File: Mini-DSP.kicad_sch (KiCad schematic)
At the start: 74 parts, among them J1 9V, J2 Barrel_Jack_MountingPin, J3 MOBO_Con, SW1 USB_BOOT, SW2 USB_BOOT, U1 CS4270, U2 AMS1117-3.3, U3 W25Q128JVS, U4 AMS1117-5.0, U5 APS1604M-3SQRx-SN, U6 RP2350A-QFN60, Y1 ABM8-272-T3

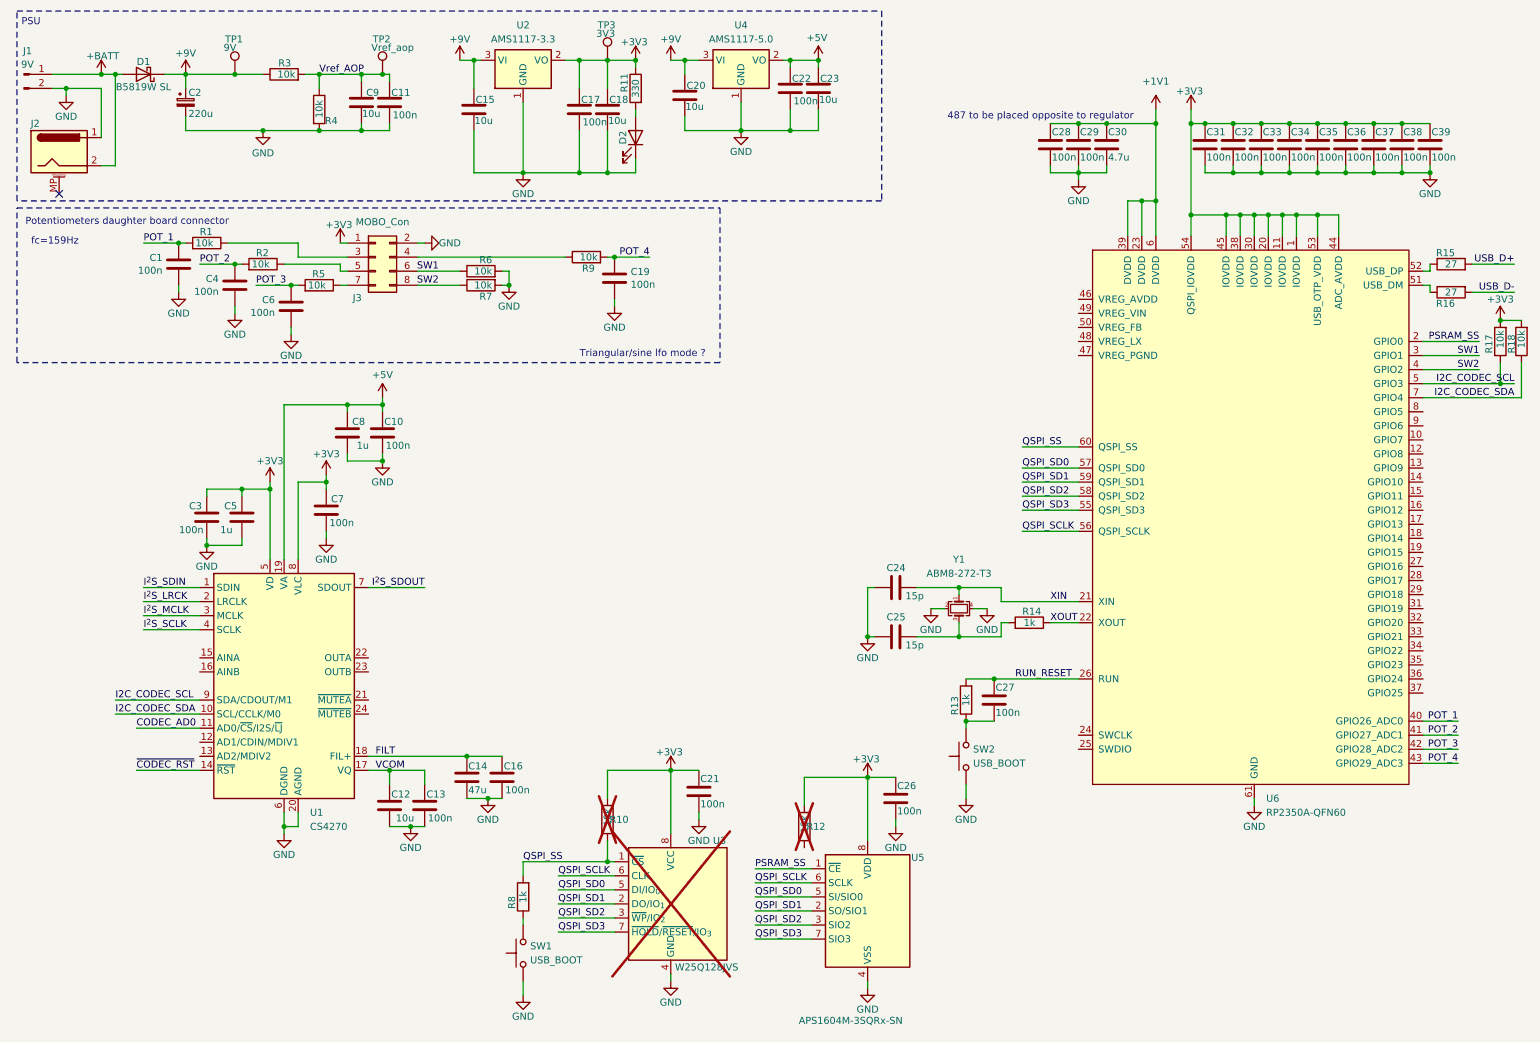
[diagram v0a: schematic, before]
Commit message: update schematic and placement
- missing 3PDT part
- need to change CS4270 (EoL)
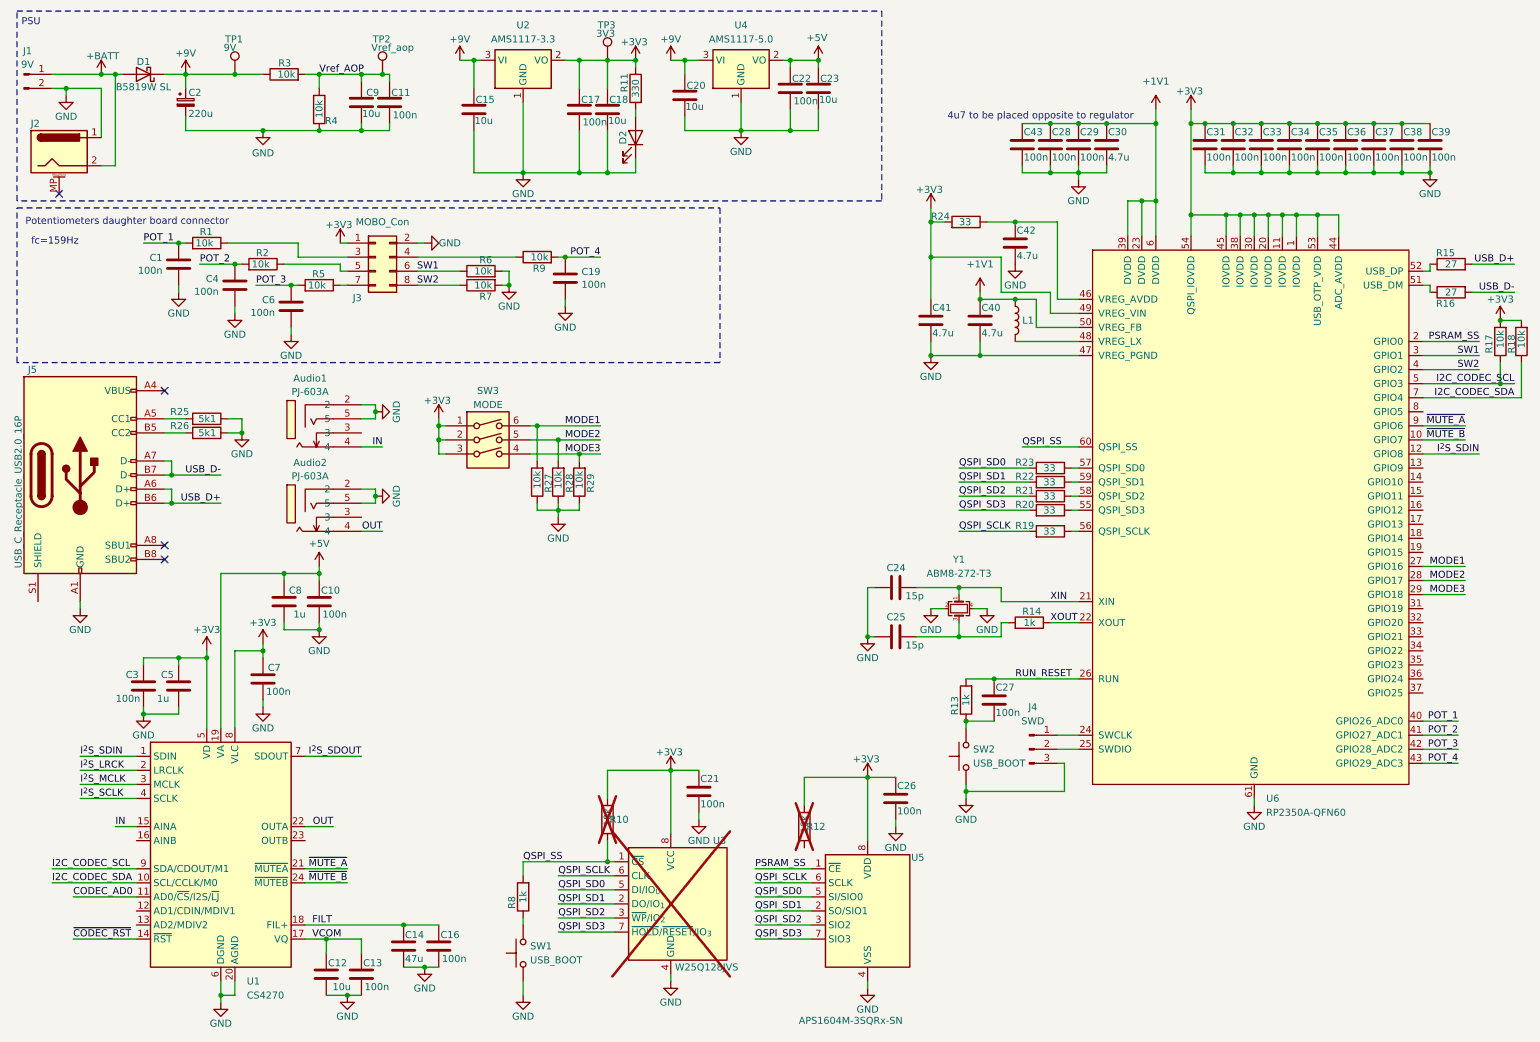
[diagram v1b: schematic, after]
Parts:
- added Audio1, Audio2: PJ-603A, easyeda2kicad:AUDIO-TH_PJ-603A, symbol easyeda2kicad:PJ-603A
- added C40, C41, C42: 4.7u, Capacitor_SMD:C_0402_1005Metric, symbol Device:C
- added C43: 100n, Capacitor_SMD:C_0402_1005Metric, symbol Device:C
- added J4: SWD, Connector_PinHeader_1.27mm:PinHeader_1x03_P1.27mm_Vertical, symbol Connector:Conn_01x03_Pin
- added J5: USB_C_Receptacle_USB2.0_16P, Connector_USB:USB_C_Receptacle_HCTL_HC-TYPE-C-16P-01A, symbol Connector:USB_C_Receptacle_USB2.0_16P
- added L1: AOTA-B201610S3R3-101-T, Inductor_SMD:L_Murata_DFE201610P, symbol Device:L
- added R19, R20, R21, R22, R23, R24: 33, Resistor_SMD:R_0402_1005Metric, symbol Device:R
- added R25, R26: 5k1, Resistor_SMD:R_0402_1005Metric, symbol Device:R
- added R27, R28, R29: 10k, Resistor_SMD:R_0402_1005Metric, symbol Device:R
- added SW3: MODE, Button_Switch_SMD:SW_DIP_SPSTx03_Slide_KingTek_DSHP03TS_W7.62mm_P1.27mm, symbol Switch:SW_DIP_x03
- C1, C11, C17, C19, C22, C4, C6: footprint Capacitor_SMD:C_0603_1608Metric -> Capacitor_SMD:C_0402_1005Metric
- C10, C13, C16, C3, C7: footprint Capacitor_SMD:C_0805_2012Metric -> Capacitor_SMD:C_0402_1005Metric
- R1, R10, R11, R12, R13, R14, R15, R16, R17, R18, R2, R3, R4, R5, R6, R7, R8, R9: footprint Resistor_SMD:R_0603_1608Metric -> Resistor_SMD:R_0402_1005Metric
- U6: footprint (none) -> Package_DFN_QFN:QFN-60-1EP_7x7mm_P0.4mm_EP3.4x3.4mm_ThermalVias
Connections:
- net +1V1: now also U6.50 (VREG_FB), C40.1, C43.1, L1.1
- net +3V3: now also U6.49 (VREG_VIN), C41.1, R24.2, SW3.1, SW3.2, SW3.3
- net GND: now also U6.47 (VREG_PGND), Audio1.2, Audio1.5, Audio2.2, Audio2.5, C40.2, C41.2, C42.2, C43.2, J4.3 (Pin_3), J5.A1 (GND), J5.A12 (GND), J5.B1 (GND), J5.B12 (GND), R25.1, R26.1, R27.1, R28.1, R29.1
- net I^{2}S_SDIN: now also U6.12 (GPIO8)
- net QSPI_SCLK: now also R19.2; no longer U6.56 (QSPI_SCLK)
- net QSPI_SD0: now also R23.2; no longer U6.57 (QSPI_SD0)
- net QSPI_SD1: now also R22.2; no longer U6.59 (QSPI_SD1)
- net QSPI_SD2: now also R21.2; no longer U6.58 (QSPI_SD2)
- net QSPI_SD3: now also R20.2; no longer U6.55 (QSPI_SD3)
- net USB_D+: now also J5.A6 (D+), J5.B6 (D+)
- net USB_D-: now also J5.A7 (D-), J5.B7 (D-)
- net ~{MUTE_B}: now reaches U6.10 (GPIO7)
- net ~{MUTE_B}: now also U1.24 (~{MUTEB})
- net at U6.24 (SWCLK): now also J4.1 (Pin_1)
- net at U6.25 (SWDIO): now also J4.2 (Pin_2)
- net MODE1: now reaches U6.27 (GPIO16)
- net MODE1: now also R27.2, SW3.6
- net MODE2: now reaches U6.28 (GPIO17)
- net MODE2: now also R28.2, SW3.5
- net MODE3: now reaches U6.29 (GPIO18)
- net MODE3: now also R29.2, SW3.4
- net at U6.46 (VREG_AVDD): now also C42.1, R24.1
- net at U6.48 (VREG_LX): now also L1.2
- net ~{MUTE_A}: now reaches U6.9 (GPIO6)
- net ~{MUTE_A}: now also U1.21 (~{MUTEA})
- net IN: now reaches U1.15 (AINA)
- net IN: now also Audio1.4
- net OUT: now reaches U1.22 (OUTA)
- net OUT: now also Audio2.4
- new net: R19.1, U6.56 (QSPI_SCLK)
- new net: R20.1, U6.55 (QSPI_SD3)
- new net: R23.1, U6.57 (QSPI_SD0)
- new net: R21.1, U6.58 (QSPI_SD2)
- new net: R22.1, U6.59 (QSPI_SD1)
- new net: J5.B5 (CC2), R26.2
- new net: J5.A4 (VBUS), J5.A9 (VBUS), J5.B4 (VBUS), J5.B9 (VBUS)
- new net: J5.A5 (CC1), R25.2
- no-connect marks 1 -> 4
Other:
- note added: "4u7 to be placed opposite to regulator"
- note removed: "487 to be placed opposite to regulator"
- note removed: "Triangular/sine lfo mode ?"
- moved on the sheet: C10, C12, C13, C14, C16, C19, C3, C5, C7, C8, R9, U1

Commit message: WIP
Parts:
- removed C22: 100n, Capacitor_SMD:C_0402_1005Metric, symbol Device:C
- removed C23: 10u, Capacitor_SMD:C_0805_2012Metric, symbol Device:C
- removed U1: CS4270, Package_SO:TSSOP-24_4.4x7.8mm_P0.65mm, symbol Audio:CS4270
- removed U4: AMS1117-5.0, Package_TO_SOT_SMD:SOT-223-3_TabPin2, symbol Regulator_Linear:AMS1117-5.0
- added C44, C49, C50: 100n, Capacitor_SMD:C_0402_1005Metric, symbol Device:C
- added C45: 10u, Capacitor_SMD:C_0603_1608Metric, symbol Device:C
- added D3: CTL1, LED_SMD:LED_0603_1608Metric, symbol Device:LED
- added R30: 330, Resistor_SMD:R_0402_1005Metric, symbol Device:R
- added U7: ES8388, Package_DFN_QFN:QFN-28-1EP_4x4mm_P0.45mm_EP2.6x2.6mm, symbol Audio:ES8388
- C10, C13, C16: value 100n -> 10u; footprint Capacitor_SMD:C_0402_1005Metric -> Capacitor_SMD:C_0603_1608Metric
- C12: value 10u -> 1u
- C14: value 47u -> 10u; footprint Capacitor_SMD:C_1206_3216Metric -> Capacitor_SMD:C_0603_1608Metric
- C15, C18, C9: footprint Capacitor_SMD:C_0805_2012Metric -> Capacitor_SMD:C_0603_1608Metric
- C20: value 10u -> 100n; footprint Capacitor_SMD:C_0805_2012Metric -> Capacitor_SMD:C_0402_1005Metric
- C5: value 1u -> 10u; footprint Capacitor_SMD:C_0805_2012Metric -> Capacitor_SMD:C_0603_1608Metric
- C7: value 100n -> 1u; footprint Capacitor_SMD:C_0402_1005Metric -> Capacitor_SMD:C_0805_2012Metric
- C8: value 1u -> 100n; footprint Capacitor_SMD:C_0805_2012Metric -> Capacitor_SMD:C_0402_1005Metric
- U6: value RP2350A-QFN60 -> RP2354A-QFN60
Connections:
- net +5V is gone; now on net +3V3: C10.1, C8.1
- net +3V3: now also C20.1, C44.1, C45.1, U7.16 (HPVDD), U7.17 (AVDD), U7.2 (DVDD), U7.3 (PVDD); no longer C7.1
- net +9V: no longer C20.1
- net GND: now also C44.2, C45.2, C49.2, C50.2, D3.1 (K), U7.13 (HPGND), U7.18 (AGND), U7.29 (EPAD), U7.4 (DGND); no longer C12.2, C7.2
- net I2C_CODEC_SCL: now also U7.27 (CDATA)
- net I2C_CODEC_SDA: now also U7.28 (CCLK)
- net IN: now also C7.2
- net I^{2}S_LRCK: now also U6.14 (GPIO10), U7.7 (LRCK)
- net I^{2}S_MCLK: now also U6.16 (GPIO12), U7.1 (MCLK)
- net I^{2}S_SCLK: now also U6.15 (GPIO11), U7.5 (SCLK)
- net I^{2}S_SDIN: now also U7.6 (DSDIN)
- net I^{2}S_SDOUT: now also U6.13 (GPIO9), U7.8 (ASDOUT)
- net OUT: now also C12.2
- net PSRAM_SS: now also R12.1
- net at U6.32 (GPIO20): now also R30.1
- net FILT: no longer names the net of C14.1
- net FILT: now also C49.1, U7.19 (ADCVREF); no longer C16.1
- net VCOM: no longer names the net of C12.1
- net VCOM: now also U7.12 (LOUT1); no longer C13.1
- new net: C13.1, U7.10 (VREF)
- new net: C16.1, C50.1, U7.20 (VMID)
- new net: C7.1, U7.24 (LIN1)
- new net: D3.2 (A), R30.2
- new net CODEC_CE: U7.26 (CE)
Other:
- moved on the sheet: C21, C24, C25, C26, C27, C28, C29, C3, C30, C31, C32, C33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
